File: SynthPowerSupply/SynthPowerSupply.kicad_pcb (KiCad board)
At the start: 2 copper layers, 38.1 x 105.4 mm, 32 parts, among them J1 Barrel_Jack_Switch, J2 Screw_Terminal_01x04, U1 LM7812_TO220, U2 LM7912_TO220, U5 LM7805_TO220

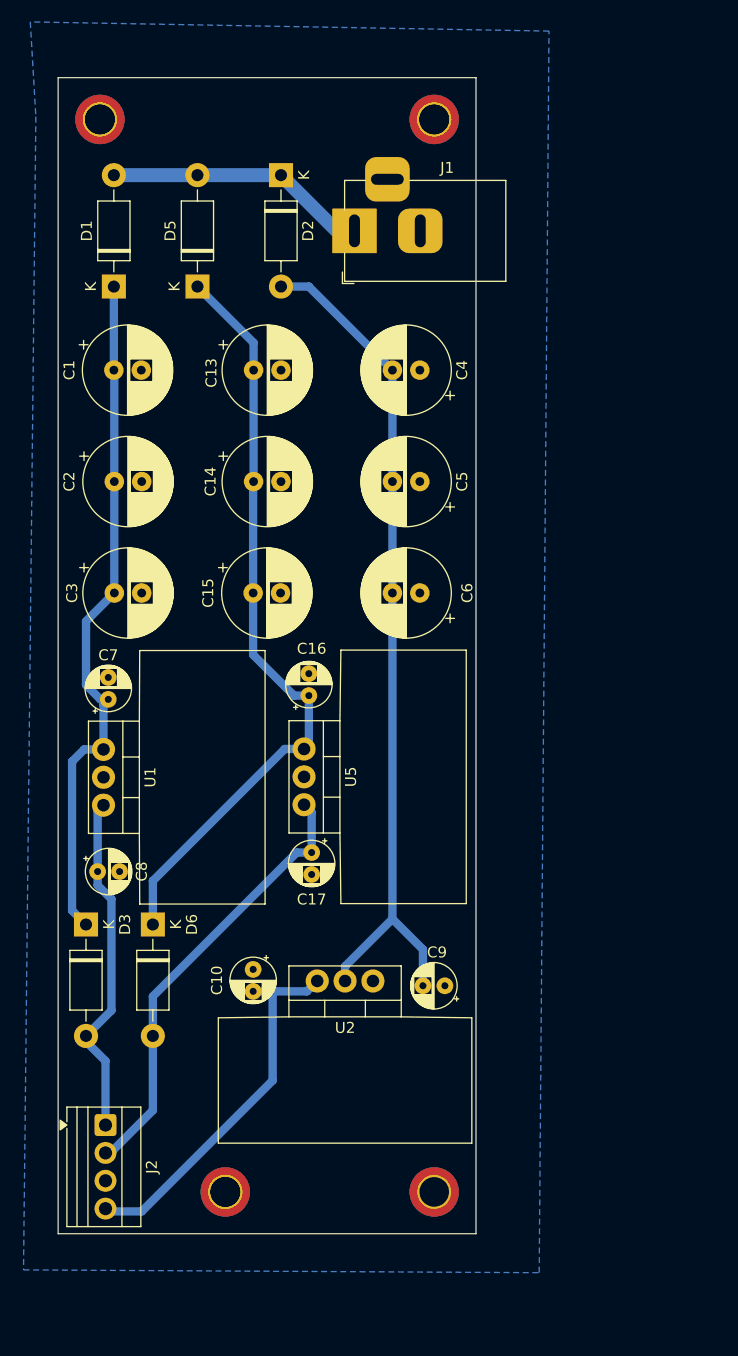
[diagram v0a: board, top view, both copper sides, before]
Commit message: Create Power supply PCB
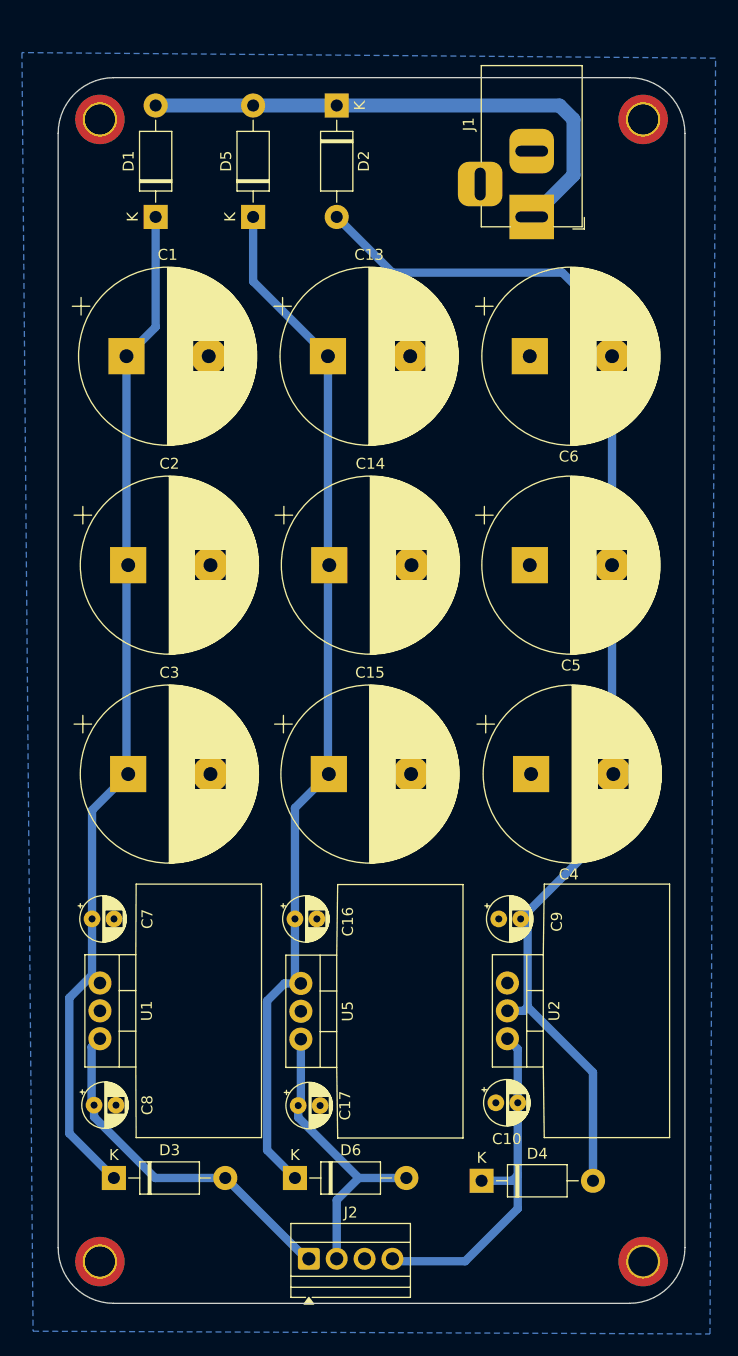
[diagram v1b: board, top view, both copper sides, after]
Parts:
- added D4: 1N4001, Diode_THT:D_DO-41_SOD81_P10.16mm_Horizontal, F.Cu at (64.0, 120.9)
- C1, C13, C14, C15, C2, C3, C4, C5, C6: footprint Capacitor_THT:CP_Radial_D8.0mm_P2.50mm -> Capacitor_THT:CP_Radial_D16.0mm_P7.50mm
- moved C4 38.2 mm to (68.5, 83.8), turned to 0 degrees
- moved D6 26.5 mm to (47.0, 120.7), turned to 0 degrees
- moved C10 25.3 mm to (65.3, 113.8), turned to 0 degrees
- moved C6 23.8 mm to (68.4, 45.7), turned to 0 degrees
- moved D3 23.3 mm to (30.5, 120.7), turned to 0 degrees
- moved C17 23.1 mm to (47.3, 114.0), turned to 0 degrees
- moved J2 22.2 mm to (48.3, 128.0), turned to 0 degrees
- moved U5 21.4 mm to (47.5, 102.9)
- moved C8 21.3 mm to (28.7, 114.0)
- moved U1 21.3 mm to (29.2, 102.9)
- moved C16 20.4 mm to (47.0, 97.0), turned to 0 degrees
- moved REF** 20.1 mm to (78.7, 128.3)
- moved C7 20.1 mm to (28.5, 97.0), turned to 0 degrees
- moved ? 19.0 mm to (78.7, 24.1)
- moved REF** 19.0 mm to (78.7, 24.1)
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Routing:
- net Net-(D2-A): track 78.1 -> 115.6 mm
- net Net-(D1-K): track 63.4 -> 93.7 mm
- net Net-(D5-K): track 70.1 -> 95.2 mm
- net Net-(D1-A): track 24.0 -> 49.1 mm
- net +5V: track 40.9 -> 27.8 mm
- net -12V: track 34.7 -> 32.8 mm
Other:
- board size 38.1 x 105.4 mm -> 57.1 x 111.8 mm
